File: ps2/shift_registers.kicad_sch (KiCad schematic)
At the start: 5 parts, among them U10 74HC195, U11 74HC195, U12 74HC280, U13 74HC541, U9 74HC195

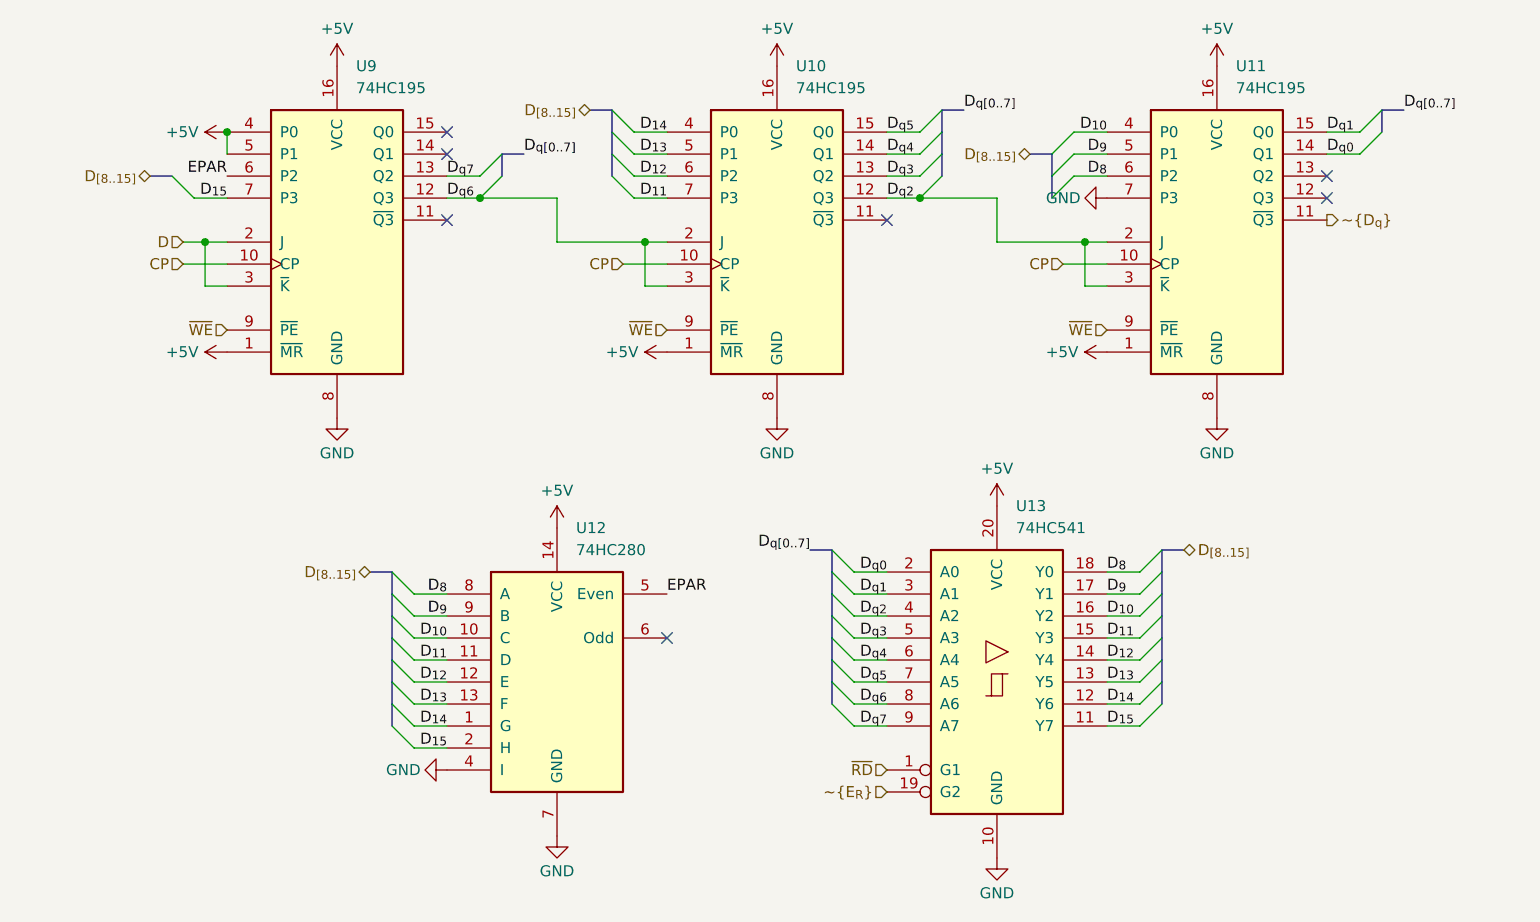
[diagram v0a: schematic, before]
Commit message: [ps2]:	made pcb design of the new latest schematic
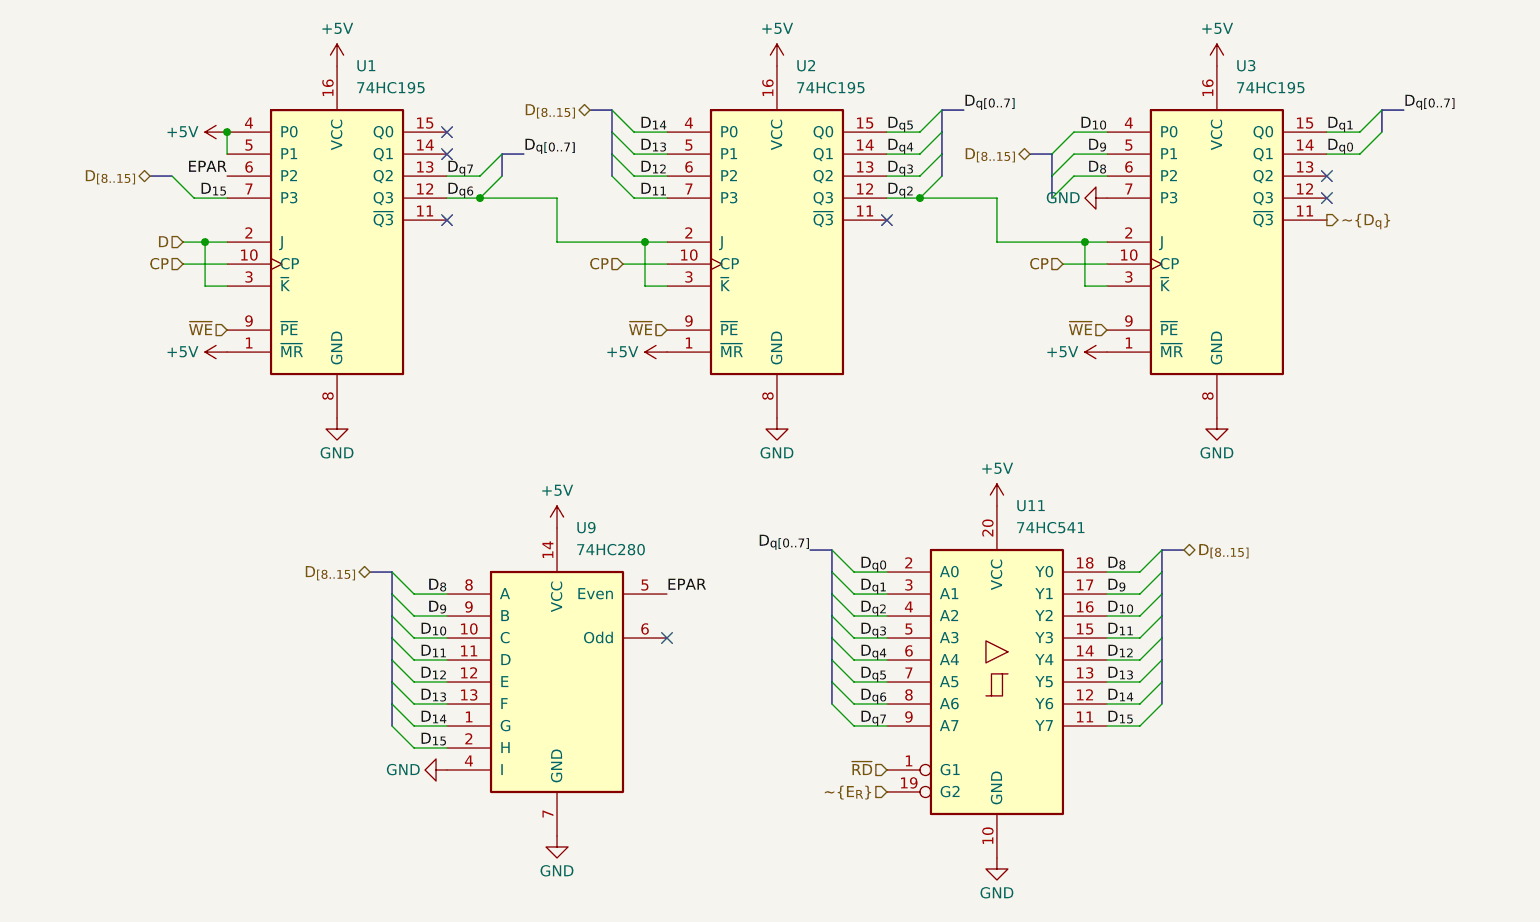
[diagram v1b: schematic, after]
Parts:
- renumbered U9 to U1, U13 to U11, U10 to U2, U11 to U3, U12 to U9
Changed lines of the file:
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@@
 		(dnp no)
 		(fields_autoplaced yes)
-		(property "Reference" "U9"
+		(property "Reference" "U1"
 			(at 103.7941 68.58 0)
 			(effects
@@
 			)
 		)
-		(property "Datasheet" "http://www.ti.com/lit/gpn/sn74LS195"
+		(property "Datasheet" ""
 			(at 101.6 88.9 0)
 			(effects
@@
 			)
 		)
-		(property "Description" "Shift Register 4-bit, parallel"
+		(property "Description" ""
 			(at 101.6 88.9 0)
 			(effects
@@
 			(project "ps2"
 				(path "/0417edbf-d6ac-46fa-bfd1-1542e1b615ef/753d7433-4eab-45b6-b955-e04603562ec7"
-					(reference "U9")
+					(reference "U1")
 					(unit 1)
 				)
@@
 		(dnp no)
 		(fields_autoplaced yes)
-		(property "Reference" "U12"
+		(property "Reference" "U9"
 			(at 129.1941 121.92 0)
 			(effects
@@
 			)
 		)
-		(property "Datasheet" "http://www.ti.com/lit/gpn/sn74LS280"
+		(property "Datasheet" ""
 			(at 127 139.7 0)
 			(effects
@@
 			)
 		)
-		(property "Description" "Parity Generator/Checker"
+		(property "Description" ""
 			(at 127 139.7 0)
 			(effects
@@
 			(project "ps2"
 				(path "/0417edbf-d6ac-46fa-bfd1-1542e1b615ef/753d7433-4eab-45b6-b955-e04603562ec7"
-					(reference "U12")
+					(reference "U9")
 					(unit 1)
 				)
@@
 		(dnp no)
 		(fields_autoplaced yes)
-		(property "Reference" "U13"
+		(property "Reference" "U11"
 			(at 179.9941 119.38 0)
 			(effects
@@
 			)
 		)
-		(property "Datasheet" "http://www.ti.com/lit/gpn/sn74LS541"
+		(property "Datasheet" ""
 			(at 177.8 139.7 0)
 			(effects
@@
 			)
 		)
-		(property "Description" "8-bit Buffer/Line Driver 3-state outputs"
+		(property "Description" ""
 			(at 177.8 139.7 0)
 			(effects
@@
 			(project "ps2"
 				(path "/0417edbf-d6ac-46fa-bfd1-1542e1b615ef/753d7433-4eab-45b6-b955-e04603562ec7"
-					(reference "U13")
+					(reference "U11")
 					(unit 1)
 				)
@@
 		(dnp no)
 		(fields_autoplaced yes)
-		(property "Reference" "U10"
+		(property "Reference" "U2"
 			(at 154.5941 68.58 0)
 			(effects
@@
 			)
 		)
-		(property "Datasheet" "http://www.ti.com/lit/gpn/sn74LS195"
+		(property "Datasheet" ""
 			(at 152.4 88.9 0)
 			(effects
@@
 			)
 		)
-		(property "Description" "Shift Register 4-bit, parallel"
+		(property "Description" ""
 			(at 152.4 88.9 0)
 			(effects
@@
 			(project "ps2"
 				(path "/0417edbf-d6ac-46fa-bfd1-1542e1b615ef/753d7433-4eab-45b6-b955-e04603562ec7"
-					(reference "U10")
+					(reference "U2")
 					(unit 1)
 				)
@@
 		(dnp no)
 		(fields_autoplaced yes)
-		(property "Reference" "U11"
+		(property "Reference" "U3"
 			(at 205.3941 68.58 0)
 			(effects
@@
 			)
 		)
-		(property "Datasheet" "http://www.ti.com/lit/gpn/sn74LS195"
+		(property "Datasheet" ""
 			(at 203.2 88.9 0)
 			(effects
@@
 			)
 		)
-		(property "Description" "Shift Register 4-bit, parallel"
+		(property "Description" ""
 			(at 203.2 88.9 0)
 			(effects
@@
 			(project "ps2"
 				(path "/0417edbf-d6ac-46fa-bfd1-1542e1b615ef/753d7433-4eab-45b6-b955-e04603562ec7"
-					(reference "U11")
-					(unit 1)
-				)
+					(reference "U3")
+					(unit 1)
+				)
